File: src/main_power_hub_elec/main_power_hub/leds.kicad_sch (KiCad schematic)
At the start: 6 parts

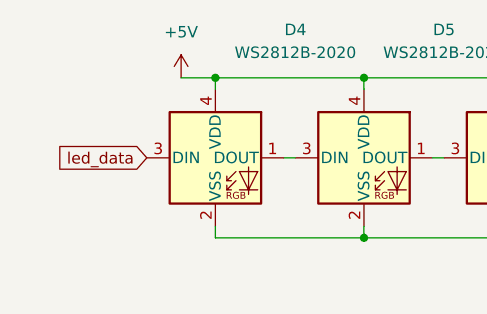
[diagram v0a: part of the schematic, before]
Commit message: Finish schematic besides bypass capacitors
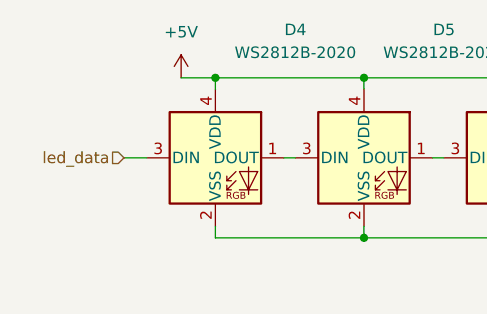
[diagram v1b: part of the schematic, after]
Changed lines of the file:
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@@
+	(wire
+		(pts
+			(xy 97.79 88.9) (xy 100.33 88.9)
+		)
+		(stroke
+			(width 0)
+			(type default)
+		)
+	)
 	(wire
 		(pts
@@
 		)
 	)
-	(global_label "led_data"
+	(hierarchical_label "led_data"
 		(shape input)
-		(at 100.33 88.9 180)
-		(fields_autoplaced yes)
+		(at 97.79 88.9 180)
 		(effects
 			(font
@@
 			(justify right)
 		)
-		(property "Intersheetrefs" "${INTERSHEET_REFS}"
-			(at 89.3017 88.9 0)
-			(effects
-				(font
-					(size 1.27 1.27)
-				)
-				(justify right)
-				(hide yes)
-			)
-		)
 	)
